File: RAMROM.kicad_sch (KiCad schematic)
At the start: 10 parts, among them U10 39SF040, U11 39SF040, U8 KM48C2100, U9 KM48C2100

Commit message: idk
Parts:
- added R30, R31: 1k, stdpads:R_0603, symbol Device:R_Small
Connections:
- net GND: now also R30.1
- net ROM~{WE}: now also R31.1
- net ~{OE}: now also R30.2
- new net +3V3: R31.2

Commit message: Before switching to SiT2001 oscillator
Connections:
- net +3V3 is gone; now on net +5V: R31.2
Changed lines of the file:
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@@
-	)
-	(symbol
-		(lib_id "power:+3V3")
-		(at 115.57 138.43 0)
-		(unit 1)
-		(exclude_from_sim no)
-		(in_bom yes)
-		(on_board yes)
-		(dnp no)
-		(property "Reference" "#PWR042"
-			(at 115.57 142.24 0)
-			(effects
-				(font
-					(size 1.27 1.27)
-				)
-				(hide yes)
-			)
-		)
-		(property "Value" "+3V3"
-			(at 115.57 134.62 0)
-			(effects
-				(font
-					(size 1.27 1.27)
-				)
-			)
-		)
-		(property "Footprint" ""
-			(at 115.57 138.43 0)
-			(effects
-				(font
-					(size 1.27 1.27)
-				)
-				(hide yes)
-			)
-		)
-		(property "Datasheet" ""
-			(at 115.57 138.43 0)
-			(effects
-				(font
-					(size 1.27 1.27)
-				)
-				(hide yes)
-			)
-		)
-		(property "Description" "Power symbol creates a global label with name \"+3V3\""
-			(at 115.57 138.43 0)
-			(effects
-				(font
-					(size 1.27 1.27)
-				)
-				(hide yes)
-			)
-		)
-		(pin "1"
-		)
-		(instances
-			(project ""
-				(path "/a5be2cb8-c68d-4180-8412-69a6b4c5b1d4/00000000-0000-0000-0000-00005f723900"
-					(reference "#PWR042")
-					(unit 1)
-				)
-			)
-		)
 	)
 	(symbol
@@
 					(unit 1)
 				)
+			)
+		)
+	)
+	(symbol
+		(lib_id "power:+5V")
+		(at 115.57 138.43 0)
+		(unit 1)
+		(exclude_from_sim no)
+		(in_bom yes)
+		(on_board yes)
+		(dnp no)
+		(property "Reference" "#PWR042"
+			(at 115.57 142.24 0)
+			(effects
+				(font
+					(size 1.27 1.27)
+				)
+				(hide yes)
+			)
+		)
+		(property "Value" "+5V"
+			(at 115.57 134.62 0)
+			(effects
+				(font
+					(size 1.27 1.27)
+				)
+			)
+		)
+		(property "Footprint" ""
+			(at 115.57 138.43 0)
+			(effects
+				(font
+					(size 1.27 1.27)
+				)
+				(hide yes)
+			)
+		)
+		(property "Datasheet" ""
+			(at 115.57 138.43 0)
+			(effects
+				(font
+					(size 1.27 1.27)
+				)
+				(hide yes)
+			)
+		)
+		(property "Description" ""
+			(at 115.57 138.43 0)
+			(effects
+				(font
+					(size 1.27 1.27)
+				)
+				(hide yes)
+			)
+		)
+		(pin "1"
+		)
+		(instances
+			(project "WarpSE"
+				(path "/a5be2cb8-c68d-4180-8412-69a6b4c5b1d4/00000000-0000-0000-0000-00005f723900"
+					(reference "#PWR042")
+					(unit 1)
+				)

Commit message: Board changes
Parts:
- added R38, R39: 1k, stdpads:R_0603, symbol Device:R_Small
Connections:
- net +5V: now also R38.2, R39.2
- net GND: now also U8.8 (A11/NC), U9.8 (A11/NC)
- net RA0: now also U9.12 (A2); no longer U9.11 (A1)
- net RA1: now also U9.11 (A1); no longer U9.10 (A0)
- net RA10: now also U9.9 (A10); no longer U9.12 (A2)
- net RA2: now also U9.10 (A0); no longer U9.9 (A10)
- net RA3: now also U9.13 (A3); no longer U9.8 (A11/NC)
- net RA8: no longer U10.28 (A13), U11.26 (A9)
- net RA11 renamed BA19
- net BA19: now also R39.1; no longer U8.8 (A11/NC), U9.13 (A3)
- new net BA18: R38.1, U10.28 (A13), U11.26 (A9)

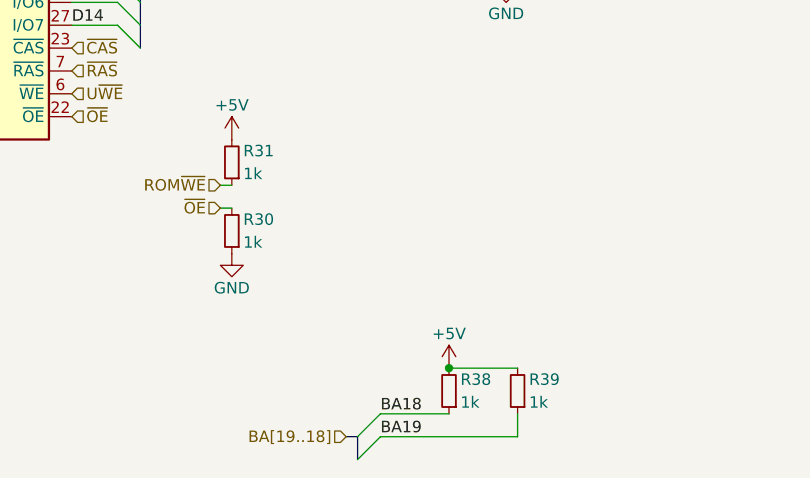
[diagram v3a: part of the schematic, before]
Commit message: Before remove first clock input buffer
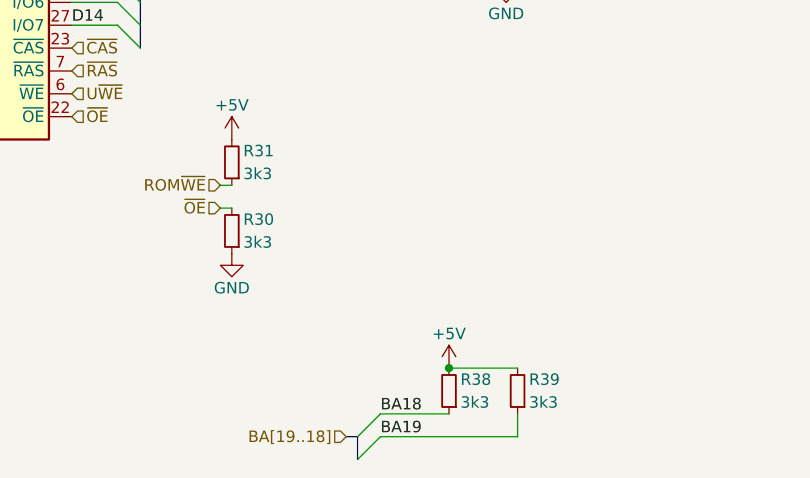
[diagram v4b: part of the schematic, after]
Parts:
- R30, R31, R38, R39: value 1k -> 3k3
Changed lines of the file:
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@@
 			)
 		)
-		(property "Value" "1k"
+		(property "Value" "3k3"
 			(at 116.84 142.24 0)
 			(effects
@@
 			)
 		)
-		(property "Value" "1k"
+		(property "Value" "3k3"
 			(at 140.97 167.64 0)
 			(effects
@@
 			)
 		)
-		(property "Value" "1k"
+		(property "Value" "3k3"
 			(at 116.84 149.86 0)
 			(effects
@@
 			)
 		)
-		(property "Value" "1k"
+		(property "Value" "3k3"
 			(at 148.59 167.64 0)
 			(effects

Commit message: Final A?
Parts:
- R30: value 3k3 -> DNP; LCSC Part C21190 -> (none)
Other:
- moved on the sheet: C16, C17
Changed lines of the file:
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@@
 	(generator "eeschema")
 	(generator_version "8.0")
-	(paper "A4")
+	(paper "USLetter")
 	(title_block
 		(title "WarpSE (GW4410A)")
-		(date "2024-04-23")
+		(date "2025-01-05")
 		(rev "1.0")
 		(company "Garrett's Workshop")
 	)
 	(junction
-		(at 265.43 111.76)
+		(at 153.67 144.78)
 		(diameter 0)
 		(color 0 0 0 0)
@@
 	)
 	(junction
-		(at 255.27 106.68)
+		(at 143.51 139.7)
 		(diameter 0)
 		(color 0 0 0 0)
@@
 	(wire
 		(pts
-			(xy 255.27 106.68) (xy 265.43 106.68)
+			(xy 143.51 139.7) (xy 153.67 139.7)
 		)
 		(stroke
@@
 	(wire
 		(pts
-			(xy 255.27 111.76) (xy 265.43 111.76)
+			(xy 143.51 144.78) (xy 153.67 144.78)
 		)
 		(stroke
@@
 	(symbol
 		(lib_id "power:+5V")
-		(at 255.27 106.68 0)
+		(at 143.51 139.7 0)
 		(unit 1)
 		(exclude_from_sim no)
@@
 		(dnp no)
 		(property "Reference" "#PWR0145"
-			(at 255.27 110.49 0)
+			(at 143.51 143.51 0)
 			(effects
 				(font
@@
 		)
 		(property "Value" "+5V"
-			(at 255.27 102.87 0)
+			(at 143.51 135.89 0)
 			(effects
 				(font
@@
 		)
 		(property "Footprint" ""
-			(at 255.27 106.68 0)
+			(at 143.51 139.7 0)
 			(effects
 				(font
@@
 		)
 		(property "Datasheet" ""
-			(at 255.27 106.68 0)
+			(at 143.51 139.7 0)
 			(effects
 				(font
@@
 		)
 		(property "Description" ""
-			(at 255.27 106.68 0)
+			(at 143.51 139.7 0)
 			(effects
 				(font
@@
 	(symbol
 		(lib_id "Device:C_Small")
-		(at 265.43 109.22 0)
+		(at 153.67 142.24 0)
 		(unit 1)
 		(exclude_from_sim no)
@@
 		(dnp no)
 		(property "Reference" "C17"
-			(at 266.7 107.95 0)
+			(at 154.94 140.97 0)
 			(effects
 				(font
@@
 		)
 		(property "Value" "10u"
-			(at 266.7 110.49 0)
+			(at 154.94 143.51 0)
 			(effects
 				(font
@@
 		)
 		(property "Footprint" "stdpads:C_0805"
-			(at 265.43 109.22 0)
+			(at 153.67 142.24 0)
 			(effects
 				(font
@@
 		)
 		(property "Datasheet" ""
-			(at 265.43 109.22 0)
+			(at 153.67 142.24 0)
 			(effects
 				(font
@@
 		)
 		(property "Description" ""
-			(at 265.43 109.22 0)
+			(at 153.67 142.24 0)
 			(effects
 				(font
@@
 		)
 		(property "LCSC Part" "C15850"
-			(at 265.43 109.22 0)
+			(at 153.67 142.24 0)
 			(effects
 				(font
@@
 	(symbol
 		(lib_id "Device:C_Small")
-		(at 255.27 109.22 0)
+		(at 143.51 142.24 0)
 		(unit 1)
 		(exclude_from_sim no)
@@
 		(dnp no)
 		(property "Reference" "C16"
-			(at 256.54 107.95 0)
+			(at 144.78 140.97 0)
 			(effects
 				(font
@@
 		)
 		(property "Value" "10u"
-			(at 256.54 110.49 0)
+			(at 144.78 143.51 0)
 			(effects
 				(font
@@
 		)
 		(property "Footprint" "stdpads:C_0805"
-			(at 255.27 109.22 0)
+			(at 143.51 142.24 0)
 			(effects
 				(font
@@
 		)
 		(property "Datasheet" ""
-			(at 255.27 109.22 0)
+			(at 143.51 142.24 0)
 			(effects
 				(font
@@
 		)
 		(property "Description" ""
-			(at 255.27 109.22 0)
+			(at 143.51 142.24 0)
 			(effects
 				(font
@@
 		)
 		(property "LCSC Part" "C15850"
-			(at 255.27 109.22 0)
+			(at 143.51 142.24 0)
 			(effects
 				(font
@@
 			)
 		)
-		(property "Value" "3k3"
+		(property "Value" "DNP"
 			(at 116.84 149.86 0)
 			(effects
@@
 			)
 		)
-		(property "LCSC Part" "C21190"
+		(property "LCSC Part" ""
 			(at 115.57 148.59 0)
 			(effects
@@
 	(symbol
 		(lib_id "power:GND")
-		(at 265.43 111.76 0)
+		(at 153.67 144.78 0)
 		(unit 1)
 		(exclude_from_sim no)
@@
 		(dnp no)
 		(property "Reference" "#PWR0135"
-			(at 265.43 118.11 0)
+			(at 153.67 151.13 0)
 			(effects
 				(font
@@
 		)
 		(property "Value" "GND"
-			(at 265.43 115.57 0)
+			(at 153.67 148.59 0)
 			(effects
 				(font
@@
 		)
 		(property "Footprint" ""
-			(at 265.43 111.76 0)
+			(at 153.67 144.78 0)
 			(effects
 				(font
@@
 		)
 		(property "Datasheet" ""
-			(at 265.43 111.76 0)
+			(at 153.67 144.78 0)
 			(effects
 				(font
@@
 		)
 		(property "Description" ""
-			(at 265.43 111.76 0)
+			(at 153.67 144.78 0)
 			(effects
 				(font
